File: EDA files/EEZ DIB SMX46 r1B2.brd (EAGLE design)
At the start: 146 x 95 mm, 157 parts, among them IC1 STM32F030C6T6, IC2 74HC1G126GW,125, IC3 M24C32-WMN6P, IC4 LP2985-33DBVR, IC5 74HC2G04GW,125, IC6 OPA2170, K1 FTR-C1GA012G-B05, K10 FTR-C1GA012G-B05, K11 FTR-C1GA012G-B05, K12 FTR-C1GA012G-B05, K13 FTR-C1GA012G-B05, K14 FTR-C1GA012G-B05, K15 FTR-C1GA012G-B05, K16 FTR-C1GA012G-B05, K17 FTR-C1GA012G-B05, K18 FTR-C1GA012G-B05, K19 FTR-C1GA012G-B05, K2 FTR-C1GA012G-B05, K20 FTR-C1GA012G-B05, K21 FTR-C1GA012G-B05, K22 FTR-C1GA012G-B05, K23 FTR-C1GA012G-B05, K24 FTR-C1GA012G-B05, K3 FTR-C1GA012G-B05, K4 FTR-C1GA012G-B05, K5 FTR-C1GA012G-B05, K6 FTR-C1GA012G-B05, K7 FTR-C1GA012G-B05, K8 FTR-C1GA012G-B05, K9 FTR-C1GA012G-B05, Q1 2N7002, Q10 2N7002, Q11 2N7002, Q12 2N7002, Q13 2N7002, Q14 2N7002, Q15 2N7002, Q16 2N7002, Q17 2N7002, Q18 2N7002, Q19 2N7002, Q2 2N7002, Q20 2N7002, Q21 2N7002, Q22 2N7002, Q23 2N7002, Q24 2N7002, Q25 2N7002, Q3 2N7002, Q4 2N7002, Q5 2N7002, Q6 2N7002, Q7 2N7002, Q8 2N7002, Q9 2N7002, X1 SSW-106-02-S-S, X2 77317-104-28LF, X3 691327310016, X4 691327310016

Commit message: #1, #2 fixed
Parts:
- C2, C9: device rcl:C1206 -> rcl:C0805
- moved C2 0.51 mm to (117.2, 20.6)
- moved C9 0.44 mm to (81.5, 15.1)
- moved C1 0.13 mm to (117.6, 22.5)
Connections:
- net +3V3: now also IC1.9; no longer IC1.8
- net BOOT0: now also X2.26
- net GND: now also IC1.8; no longer IC1.9, X2.26
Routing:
- net BOOT0: track 28.1 -> 46.9 mm, vias 3 -> 4
- net N$68: track 95.7 -> 94.7 mm

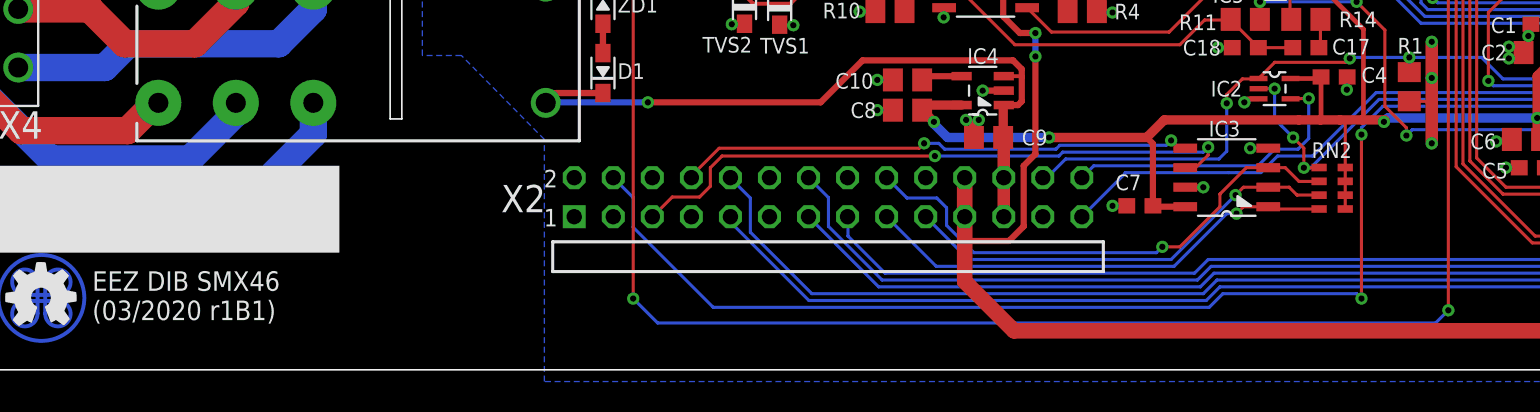
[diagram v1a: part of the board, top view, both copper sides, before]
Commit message: swap UART TX and RX
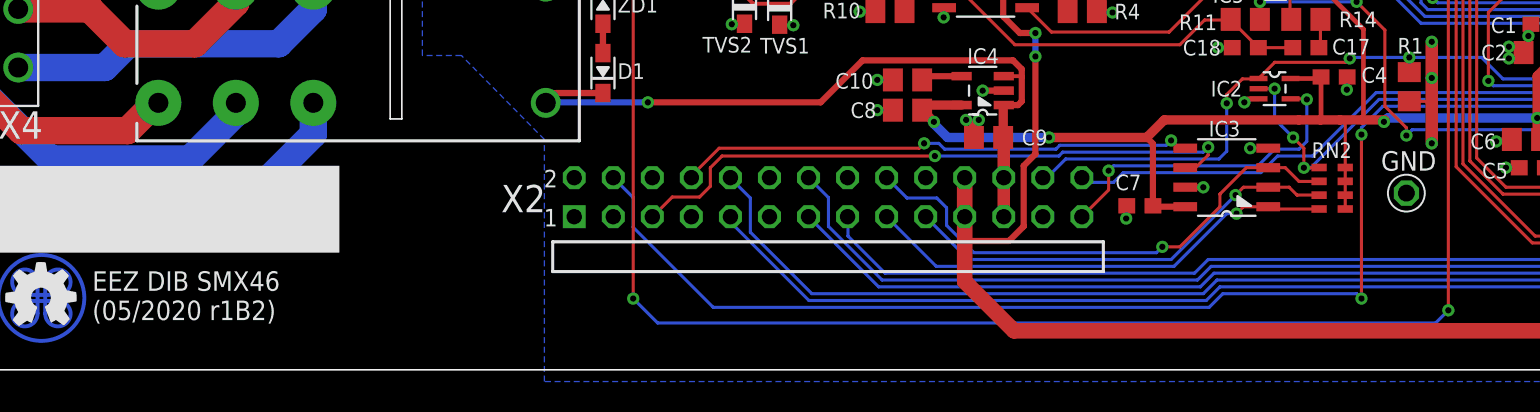
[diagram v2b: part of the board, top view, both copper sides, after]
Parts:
- added GND: (no value), EEZ_Lib1:PCB_SHIELD_TAB
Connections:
- net GND: now also GND.1
- net N$72: now also X2.27; no longer X2.28
- net UART_RX: now also X2.28; no longer X2.27
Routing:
- net N$72: track 19.6 -> 21.2 mm, vias 1 -> 2
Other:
- board text added: "EEZ DIB SMX46 (05/2020 r1B2)"
- board text added: "EEZ DIB SMX46 (05/2020 r1B2) Project source code: github.com/eez-open"
- board text removed: "EEZ DIB SMX46 (03/2020 r1B1)"
- board text removed: "EEZ DIB SMX46 (03/2020 r1B1) Project source code: github.com/eez-open"
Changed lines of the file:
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@@
 <layer number="20" name="Dimension" color="12" fill="1" visible="yes" active="yes"/>
 <layer number="21" name="tPlace" color="7" fill="1" visible="yes" active="yes"/>
-<layer number="22" name="bPlace" color="6" fill="1" visible="no" active="yes"/>
+<layer number="22" name="bPlace" color="6" fill="1" visible="yes" active="yes"/>
 <layer number="23" name="tOrigins" color="15" fill="1" visible="yes" active="yes"/>
 <layer number="24" name="bOrigins" color="15" fill="1" visible="no" active="yes"/>
@@
 <dimension x1="-10" y1="81" x2="-11" y2="17" x3="-12" y3="49" textsize="2" layer="47" dtype="vertical"/>
 <text x="23.1675" y="3.2345" size="1.27" layer="21" font="vector" ratio="10" rot="SR0">EEZ DIB SMX46
-(03/2020 r1B1)</text>
-<text x="143.036" y="88.642" size="1.27" layer="22" font="vector" ratio="10" rot="SMR0">EEZ DIB SMX46 (03/2020 r1B1)
+(05/2020 r1B2)</text>
+<text x="143.036" y="88.642" size="1.27" layer="22" font="vector" ratio="10" rot="SMR0">EEZ DIB SMX46 (05/2020 r1B2)
 Project source code: github.com/eez-open</text>
 <rectangle x1="17.145" y1="7.62" x2="39.243" y2="13.2715" layer="21"/>
@@
 <attribute name="VALUE" x="119.507" y="26.3525" size="1.016" layer="27" ratio="10"/>
 </element>
+<element name="GND" library="EEZ_Lib1" package="PCB_SHIELD_TAB" value="" x="108.6485" y="11.4935" smashed="yes">
+<attribute name="NAME" x="106.9975" y="12.954" size="1.27" layer="25" ratio="10"/>
+</element>
 </elements>
 <signals>
@@
 <contactref element="C8" pad="2"/>
 <via x="98.4885" y="14.4145" extent="1-16" drill="0.4" shape="square"/>
-<via x="89.535" y="10.668" extent="1-16" drill="0.4" shape="square"/>
+<via x="90.424" y="9.8425" extent="1-16" drill="0.4" shape="square"/>
 <contactref element="C7" pad="1"/>
 <contactref element="IC3" pad="7"/>
@@
 <via x="96.393" y="20.955" extent="1-16" drill="0.4" shape="square"/>
 <wire x1="97.321" y1="20.955" x2="96.393" y2="20.955" width="0.2032" layer="1"/>
-<wire x1="90.463" y1="10.668" x2="89.535" y2="10.668" width="0.4064" layer="1"/>
+<wire x1="90.463" y1="10.668" x2="90.424" y2="9.8425" width="0.4064" layer="1"/>
 <via x="95.4405" y="11.8745" extent="1-16" drill="0.4" shape="square"/>
 <wire x1="94.2645" y1="11.8795" x2="95.4355" y2="11.8795" width="0.4064" layer="1"/>
@@
 <wire x1="80.5205" y1="15.113" x2="80.5205" y2="15.941" width="0.6096" layer="1"/>
 <wire x1="80.5205" y1="15.941" x2="80.8355" y2="16.256" width="0.6096" layer="1"/>
+<contactref element="GND" pad="1"/>
 </signal>
 <signal name="N$13">
@@
 </signal>
 <signal name="UART_RX">
-<contactref element="X2" pad="27"/>
 <via x="123.698" y="18.034" extent="1-16" drill="0.4" shape="octagon"/>
 <wire x1="100.2665" y1="13.9065" x2="99.187" y2="12.827" width="0.2032" layer="16"/>
@@
 <wire x1="124.9045" y1="18.161" x2="123.825" y2="18.161" width="0.2032" layer="1"/>
 <wire x1="123.825" y1="18.161" x2="123.698" y2="18.034" width="0.2032" layer="1"/>
-<wire x1="87.54" y1="9.96" x2="90.3605" y2="12.7805" width="0.2032" layer="16"/>
-<wire x1="90.3605" y1="12.7805" x2="90.3605" y2="12.827" width="0.2032" layer="16"/>
-<wire x1="90.3605" y1="12.827" x2="97.0915" y2="12.827" width="0.2032" layer="16"/>
-<wire x1="97.0915" y1="12.827" x2="97.5995" y2="12.827" width="0.2032" layer="16"/>
-<wire x1="99.187" y1="12.827" x2="97.5995" y2="12.827" width="0.2032" layer="16"/>
+<contactref element="X2" pad="28"/>
+<wire x1="99.187" y1="12.827" x2="90.2335" y2="12.827" width="0.2032" layer="16"/>
+<wire x1="90.2335" y1="12.827" x2="89.5985" y2="12.192" width="0.2032" layer="16"/>
+<wire x1="87.7845" y1="12.2555" x2="87.54" y2="12.5" width="0.2032" layer="16"/>
+<wire x1="89.5985" y1="12.192" x2="87.848" y2="12.192" width="0.2032" layer="16"/>
+<wire x1="87.848" y1="12.192" x2="87.54" y2="12.5" width="0.2032" layer="16"/>
 </signal>
 <signal name="SWCLK">
@@
 <wire x1="129.736" y1="6.419" x2="129.7305" y2="6.4135" width="0.2032" layer="1"/>
 </signal>
-<signal name="N$72">
-<contactref element="X2" pad="28"/>
-<contactref element="IC2" pad="4"/>
-<via x="102.2985" y="17.653" extent="1-16" drill="0.4" shape="octagon"/>
-<wire x1="102.2985" y1="17.653" x2="101.1174" y2="17.6276" width="0.2032" layer="1"/>
-<wire x1="102.2985" y1="15.0495" x2="101.6" y2="14.351" width="0.2032" layer="16"/>
-<wire x1="101.6" y1="14.351" x2="100.076" y2="14.351" width="0.2032" layer="16"/>
-<wire x1="100.076" y1="14.351" x2="98.9965" y2="13.2715" width="0.2032" layer="16"/>
-<wire x1="102.2985" y1="17.653" x2="102.2985" y2="15.0495" width="0.2032" layer="16"/>
-<wire x1="98.9965" y1="13.2715" x2="88.3115" y2="13.2715" width="0.2032" layer="16"/>
-<wire x1="87.54" y1="12.5" x2="88.3115" y2="13.2715" width="0.2032" layer="16"/>
-</signal>
 <signal name="N$86">
 <contactref element="X4" pad="11"/>
@@
 <wire x1="68.961" y1="28.8925" x2="72.898" y2="28.8925" width="0.254" layer="16"/>
 </signal>
+<signal name="N$72">
+<contactref element="IC2" pad="4"/>
+<contactref element="X2" pad="27"/>
+<wire x1="101.1174" y1="17.6276" x2="102.1334" y2="17.6276" width="0.2032" layer="1"/>
+<wire x1="102.1334" y1="17.6276" x2="102.1715" y2="17.5895" width="0.2032" layer="1"/>
+<via x="102.1715" y="17.5895" extent="1-16" drill="0.4" shape="octagon"/>
+<wire x1="102.1715" y1="17.5895" x2="102.1715" y2="14.859" width="0.2032" layer="16"/>
+<wire x1="102.1715" y1="14.859" x2="101.6635" y2="14.351" width="0.2032" layer="16"/>
+<wire x1="101.6635" y1="14.351" x2="100.076" y2="14.351" width="0.2032" layer="16"/>
+<wire x1="100.076" y1="14.351" x2="98.9965" y2="13.2715" width="0.2032" layer="16"/>
+<wire x1="98.9965" y1="13.2715" x2="89.5985" y2="13.2715" width="0.2032" layer="16"/>
+<via x="89.281" y="12.954" extent="1-16" drill="0.4" shape="octagon"/>
+<wire x1="89.5985" y1="13.2715" x2="89.281" y2="12.954" width="0.2032" layer="16"/>
+<wire x1="89.281" y1="12.954" x2="89.281" y2="11.701" width="0.2032" layer="1"/>
+<wire x1="89.281" y1="11.701" x2="87.54" y2="9.96" width="0.2032" layer="1"/>
+</signal>
 </signals>

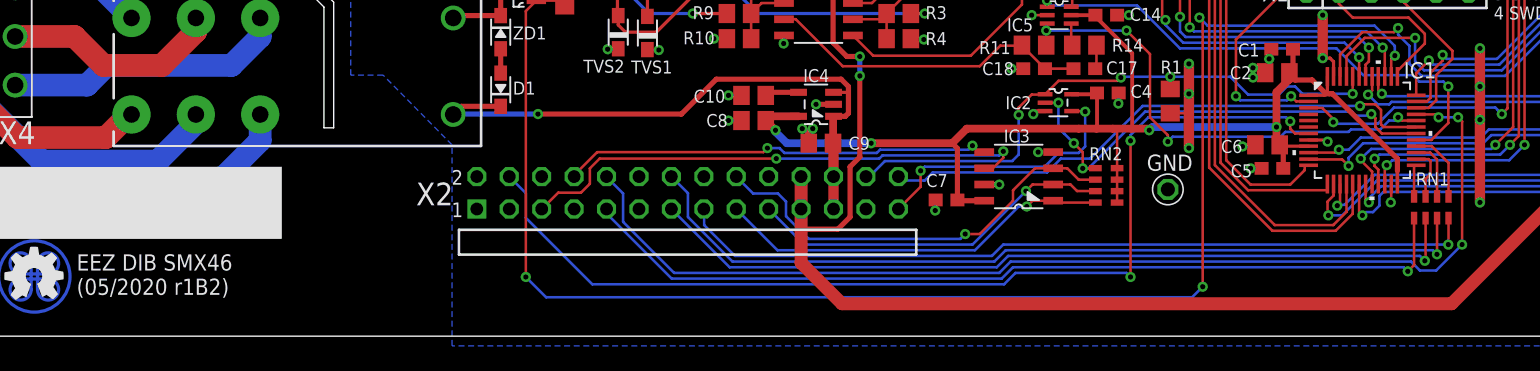
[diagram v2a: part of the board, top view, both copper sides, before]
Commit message: DIB alternative IRQs added
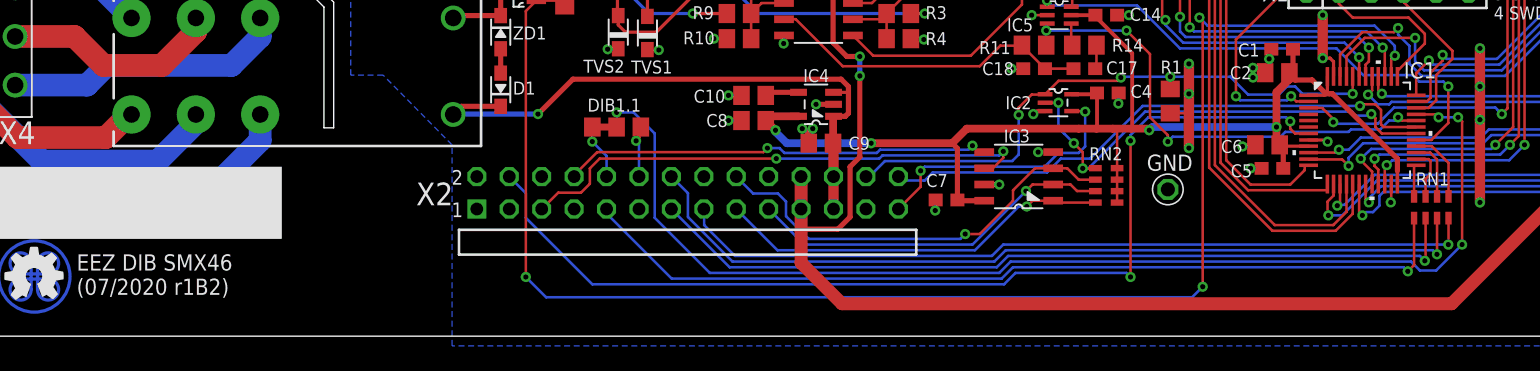
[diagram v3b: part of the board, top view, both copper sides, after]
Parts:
- added DIB1.1: JP3-CUT-0805-ROTATED, EEZ_Lib1:JP3-0805-CUT2
- X1: value SSW-106-02-S-S -> N.C.
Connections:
- new net DIB_CSB: DIB1.1.NO, X2.12
- new net N$75: DIB1.1.COM, IC1.33
- net DIB_IRQ: now also DIB1.1.NC; no longer IC1.33
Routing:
- net N$75: track 0.00 -> 91.4 mm, vias 0 -> 4
- net DIB_IRQ: track 86.4 -> 4.35 mm, vias 3 -> 1
- net DIB_CSB: track 0.00 -> 4.13 mm, vias 0 -> 1
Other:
- board text added: "EEZ DIB SMX46 (07/2020 r1B2)"
- board text added: "EEZ DIB SMX46 (07/2020 r1B2) Project source code: github.com/eez-open"
- board text removed: "EEZ DIB SMX46 (05/2020 r1B2)"
- board text removed: "EEZ DIB SMX46 (05/2020 r1B2) Project source code: github.com/eez-open"
